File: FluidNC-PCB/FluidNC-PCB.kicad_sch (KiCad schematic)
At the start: 0 parts

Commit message: First steps!
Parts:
- added A1: Pololu_Breakout_A4988, Module:Pololu_Breakout-16_15.2x20.3mm, symbol Driver_Motor:Pololu_Breakout_A4988
- added J1: Conn_01x04_Pin, symbol Connector:Conn_01x04_Pin
- added R2, R3, R4: R, symbol Device:R
- added SW1: SW_DIP_x04, Button_Switch_THT:SW_DIP_SPSTx04_Slide_9.78x12.34mm_W7.62mm_P2.54mm, symbol Switch:SW_DIP_x04
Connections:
- new net: A1.10 (MS1), R2.1, SW1.6
- new net: A1.11 (MS2), R3.1, SW1.7
- new net: A1.12 (MS3), R4.1, SW1.8
- new net: A1.3 (1B), J1.4 (Pin_4)
- new net: A1.4 (1A), J1.3 (Pin_3)
- new net: A1.5 (2A), J1.2 (Pin_2)
- new net: A1.6 (2B), J1.1 (Pin_1)
- new net +12V: A1.8 (VMOT)
- new net +3.3V: A1.13 (~{RESET}), A1.14 (~{SLEEP}), A1.2 (VDD)
- new net ENABLE_N: A1.9 (~{ENABLE})
- new net GND: A1.1 (GND), A1.7 (GND), R2.2, R3.2, R4.2
- no-connect marks 0 -> 2

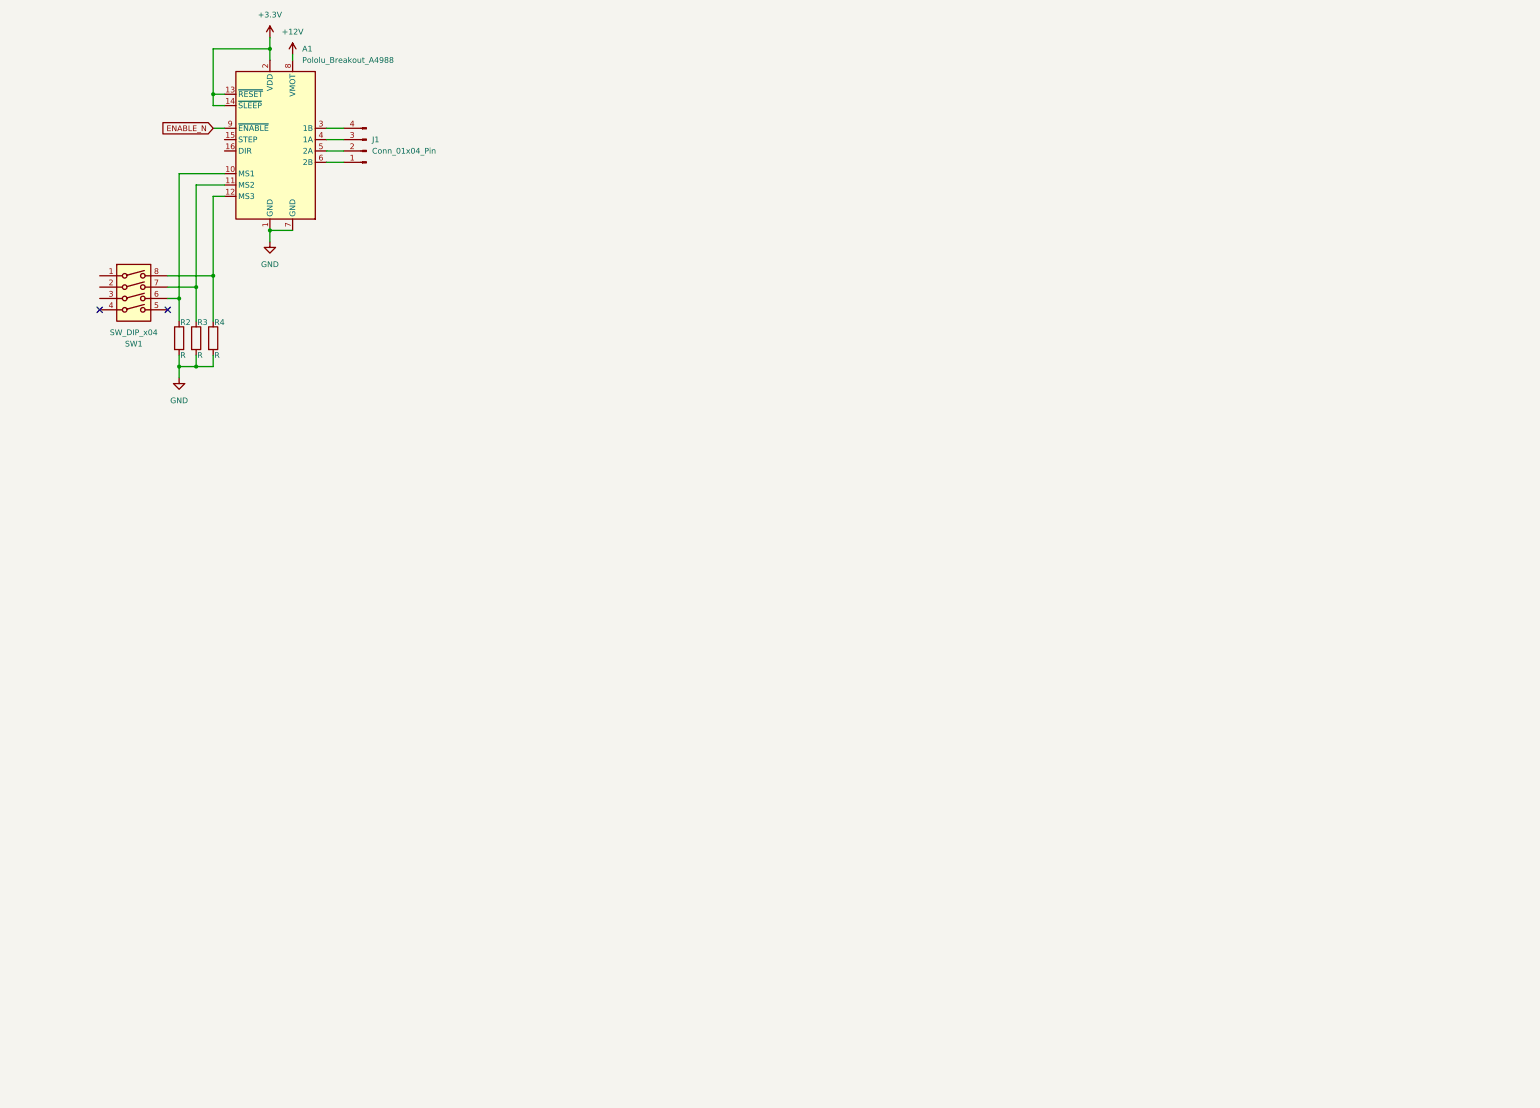
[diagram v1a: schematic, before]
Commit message: Added ESP32 plotter symbol to schematic and repo (moved from template). Started uC wiring.
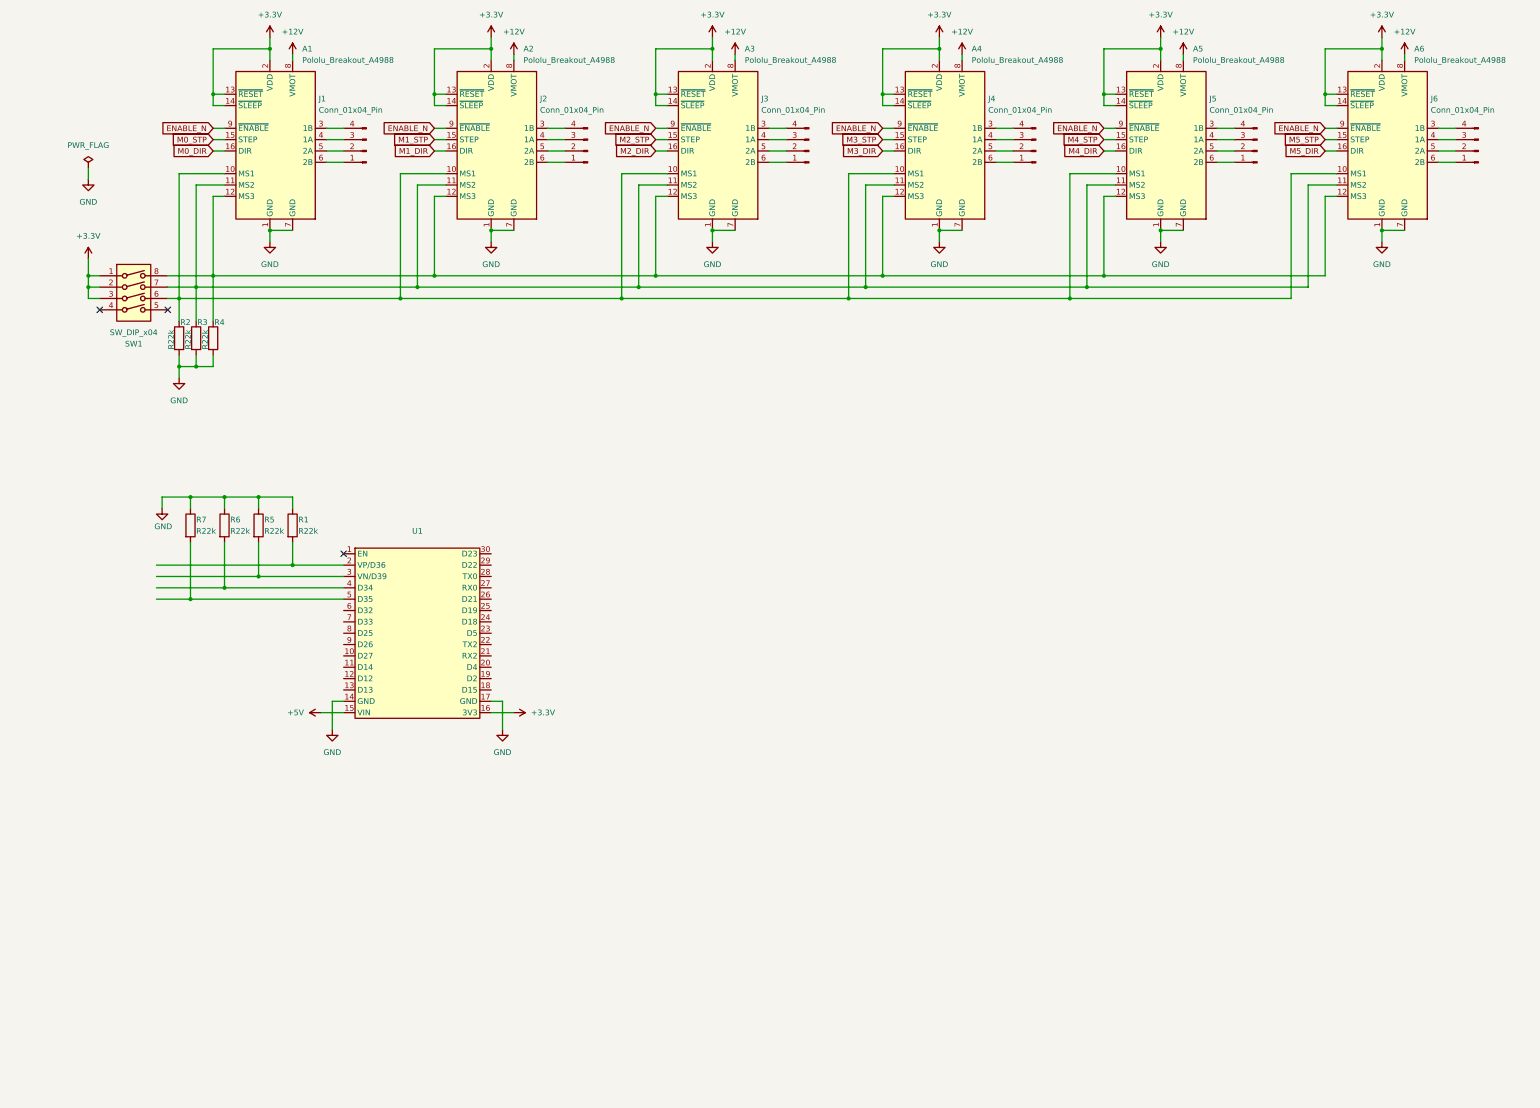
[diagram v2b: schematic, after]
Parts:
- added A2, A3, A4, A5, A6: Pololu_Breakout_A4988, Module:Pololu_Breakout-16_15.2x20.3mm, symbol Driver_Motor:Pololu_Breakout_A4988
- added J2, J3, J4, J5, J6: Conn_01x04_Pin, symbol Connector:Conn_01x04_Pin
- added R1, R5, R6, R7: R22k, symbol Device:R
- added U1: ~, plotter:esp32-mystery-footprint, symbol plotter:esp32_wroom_doit_devB
- R2, R3, R4: value R -> R22k
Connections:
- net +12V: now also A2.8 (VMOT), A3.8 (VMOT), A4.8 (VMOT), A5.8 (VMOT), A6.8 (VMOT)
- net +3.3V: now also SW1.1, SW1.2, SW1.3, A2.13 (~{RESET}), A2.14 (~{SLEEP}), A2.2 (VDD), A3.13 (~{RESET}), A3.14 (~{SLEEP}), A3.2 (VDD), A4.13 (~{RESET}), A4.14 (~{SLEEP}), A4.2 (VDD), A5.13 (~{RESET}), A5.14 (~{SLEEP}), A5.2 (VDD), A6.13 (~{RESET}), A6.14 (~{SLEEP}), A6.2 (VDD), U1.16 (3V3)
- net ENABLE_N: now also A2.9 (~{ENABLE}), A3.9 (~{ENABLE}), A4.9 (~{ENABLE}), A5.9 (~{ENABLE}), A6.9 (~{ENABLE})
- net GND: now also A2.1 (GND), A2.7 (GND), A3.1 (GND), A3.7 (GND), A4.1 (GND), A4.7 (GND), A5.1 (GND), A5.7 (GND), A6.1 (GND), A6.7 (GND), R1.1, R5.1, R6.1, R7.1, U1.14 (GND), U1.17 (GND)
- net at A1.10 (MS1), R2.1, SW1.6: now also A2.10 (MS1), A3.10 (MS1), A4.10 (MS1), A5.10 (MS1), A6.10 (MS1)
- net at A1.11 (MS2), R3.1, SW1.7: now also A2.11 (MS2), A3.11 (MS2), A4.11 (MS2), A5.11 (MS2), A6.11 (MS2)
- net at A1.12 (MS3), R4.1, SW1.8: now also A2.12 (MS3), A3.12 (MS3), A4.12 (MS3), A5.12 (MS3), A6.12 (MS3)
- net M0_STP: now reaches A1.15 (STEP)
- net M0_DIR: now reaches A1.16 (DIR)
- new net: R7.2, U1.5 (D35)
- new net: A2.3 (1B), J2.4 (Pin_4)
- new net: A2.4 (1A), J2.3 (Pin_3)
- new net: A2.5 (2A), J2.2 (Pin_2)
- new net: A2.6 (2B), J2.1 (Pin_1)
- new net: R1.2, U1.2 (VP/D36)
- new net: A4.6 (2B), J4.1 (Pin_1)
- new net: A4.5 (2A), J4.2 (Pin_2)
- new net: A4.4 (1A), J4.3 (Pin_3)
- new net: A4.3 (1B), J4.4 (Pin_4)
- new net: A6.3 (1B), J6.4 (Pin_4)
- new net: A6.4 (1A), J6.3 (Pin_3)
- new net: A6.5 (2A), J6.2 (Pin_2)
- new net: A6.6 (2B), J6.1 (Pin_1)
- new net: R5.2, U1.3 (VN/D39)
- new net: R6.2, U1.4 (D34)
- new net: A5.6 (2B), J5.1 (Pin_1)
- new net: A5.5 (2A), J5.2 (Pin_2)
- new net: A5.4 (1A), J5.3 (Pin_3)
- new net: A5.3 (1B), J5.4 (Pin_4)
- new net: A3.6 (2B), J3.1 (Pin_1)
- new net: A3.5 (2A), J3.2 (Pin_2)
- new net: A3.4 (1A), J3.3 (Pin_3)
- new net: A3.3 (1B), J3.4 (Pin_4)
- new net +5V: U1.15 (VIN)
- new net M1_DIR: A2.16 (DIR)
- new net M1_STP: A2.15 (STEP)
- new net M2_DIR: A3.16 (DIR)
- new net M2_STP: A3.15 (STEP)
- new net M3_DIR: A4.16 (DIR)
- new net M3_STP: A4.15 (STEP)
- new net M4_DIR: A5.16 (DIR)
- new net M4_STP: A5.15 (STEP)
- new net M5_DIR: A6.16 (DIR)
- new net M5_STP: A6.15 (STEP)
- no-connect marks 2 -> 3

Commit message: Mostly done PCB :)
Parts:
- removed U1: ~, plotter:esp32-mystery-footprint, symbol plotter:esp32_wroom_doit_devB
- added C1, C14, C2, C3, C4, C5, C6: 33uF, Capacitor_THT:C_Radial_D8.0mm_H11.5mm_P3.50mm, symbol Device:C
- added C10, C11, C12, C13, C7, C8, C9: 100nF, Capacitor_THT:C_Disc_D4.3mm_W1.9mm_P5.00mm, symbol Device:C
- added H1, H2, H3, H4, H5, H6: MountingHole, MountingHole:MountingHole_3.2mm_M3, symbol Mechanical:MountingHole
- added J11, J12, J13, J14, J15, J16, J17, J18, J19: Molex_01x02_Socket, Connector_Molex:Molex_KK-254_AE-6410-02A_1x02_P2.54mm_Vertical, symbol Connector:Conn_01x02_Socket
- added J7: 12V Power Input, TerminalBlock_Phoenix:TerminalBlock_Phoenix_MKDS-1,5-2_1x02_P5.00mm_Horizontal, symbol Connector:Screw_Terminal_01x02
- added J8: Fan Screw Terminal, TerminalBlock_Phoenix:TerminalBlock_Phoenix_MKDS-1,5-2_1x02_P5.00mm_Horizontal, symbol Connector:Screw_Terminal_01x02
- added R8, R9: R22k, Resistor_THT:R_Axial_DIN0207_L6.3mm_D2.5mm_P5.08mm_Vertical, symbol Device:R
- added U2: ~, plotter:esp32-mystery-footprint, symbol plotter:esp32_wroom_doit_devB
- J1, J2, J3, J4, J5, J6: footprint (none) -> Connector_Molex:Molex_KK-254_AE-6410-04A_1x04_P2.54mm_Vertical
- R1, R2, R3, R4, R5, R6, R7: footprint (none) -> Resistor_THT:R_Axial_DIN0207_L6.3mm_D2.5mm_P5.08mm_Vertical
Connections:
- net +12V: now also C1.1, C14.1, C2.1, C3.1, C4.1, C5.1, C6.1, J17.1 (Pin_1), J7.1 (Pin_1), J8.1 (Pin_1)
- net +3.3V: now also C10.1, C11.1, C12.1, C7.1, C8.1, C9.1, J11.1 (Pin_1), J12.1 (Pin_1), J13.1 (Pin_1), J14.1 (Pin_1), J15.1 (Pin_1), J16.1 (Pin_1), U2.16 (3V3)
- net +5V: now also C13.1, J18.1 (Pin_1), U2.15 (VIN)
- net ENABLE_N: now also U2.20 (D4)
- net GND: now also C1.2, C10.2, C11.2, C12.2, C13.2, C14.2, C2.2, C3.2, C4.2, C5.2, C6.2, C7.2, C8.2, C9.2, J17.2 (Pin_2), J18.2 (Pin_2), J7.2 (Pin_2), J8.2 (Pin_2), R8.2, R9.2, U2.14 (GND), U2.17 (GND)
- net M0_DIR: now also U2.6 (D32)
- net M0_STP: now also U2.7 (D33)
- net M1_DIR: now also U2.8 (D25)
- net M1_STP: now also U2.9 (D26)
- net M2_DIR: now also U2.10 (D27)
- net M2_STP: now also U2.11 (D14)
- net M3_DIR: now also U2.12 (D12)
- net M3_STP: now also U2.13 (D13)
- net M4_DIR: now also U2.30 (D23)
- net M4_STP: now also U2.29 (D22)
- net M5_DIR: now also U2.26 (D21)
- net M5_STP: now also U2.25 (D19)
- net at R7.2: now also J14.2 (Pin_2), U2.5 (D35)
- net at R1.2: now also J11.2 (Pin_2), U2.2 (VP/D36)
- net at R5.2: now also J12.2 (Pin_2), U2.3 (VN/D39)
- net at R6.2: now also J13.2 (Pin_2), U2.4 (D34)
- new net: J16.2 (Pin_2), R9.1, U2.19 (D2)
- new net: J15.2 (Pin_2), R8.1, U2.18 (D15)
- new net: J19.2 (Pin_2), U2.23 (D5)
- new net: J19.1 (Pin_1), U2.24 (D18)
- no-connect marks 3 -> 7
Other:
- note added: "Caps on drivers, uC, big caps on 12V!"
- moved on the sheet: R1, R5, R6, R7

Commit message: Finished (version 1) of PCB
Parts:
- removed H5, H6: MountingHole, MountingHole:MountingHole_3.2mm_M3, symbol Mechanical:MountingHole
- removed J19: Molex_01x02_Socket, Connector_Molex:Molex_KK-254_AE-6410-02A_1x02_P2.54mm_Vertical, symbol Connector:Conn_01x02_Socket
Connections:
- net M0_DIR: now also U2.8 (D25); no longer U2.6 (D32)
- net M0_STP: now also U2.9 (D26); no longer U2.7 (D33)
- net M1_DIR: now also U2.10 (D27); no longer U2.8 (D25)
- net M1_STP: now also U2.11 (D14); no longer U2.9 (D26)
- net M2_DIR: now also U2.12 (D12); no longer U2.10 (D27)
- net M2_STP: now also U2.13 (D13); no longer U2.11 (D14)
- net M3_DIR: now also U2.6 (D32); no longer U2.12 (D12)
- net M3_STP: now also U2.7 (D33); no longer U2.13 (D13)
- net M4_DIR: now also U2.29 (D22); no longer U2.30 (D23)
- net M4_STP: now also U2.30 (D23); no longer U2.29 (D22)
- net M5_DIR: now also U2.25 (D19); no longer U2.26 (D21)
- net M5_STP: now also U2.26 (D21); no longer U2.25 (D19)
- no-connect marks 7 -> 9

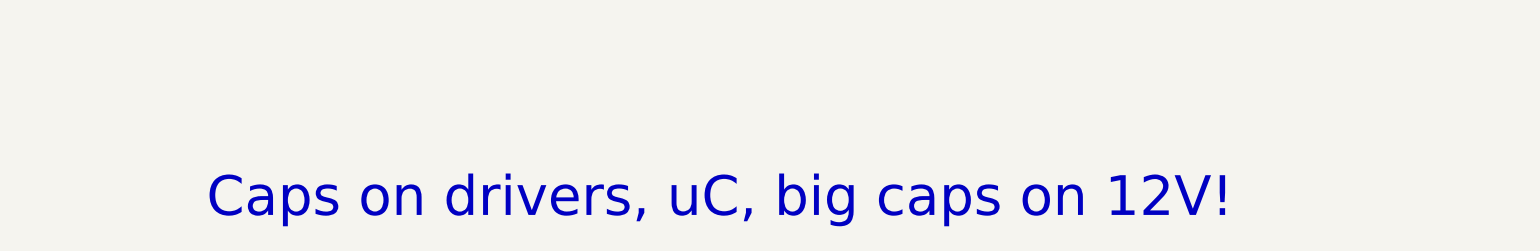
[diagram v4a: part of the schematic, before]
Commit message: Added schematic PDF and PNG of PCB layout
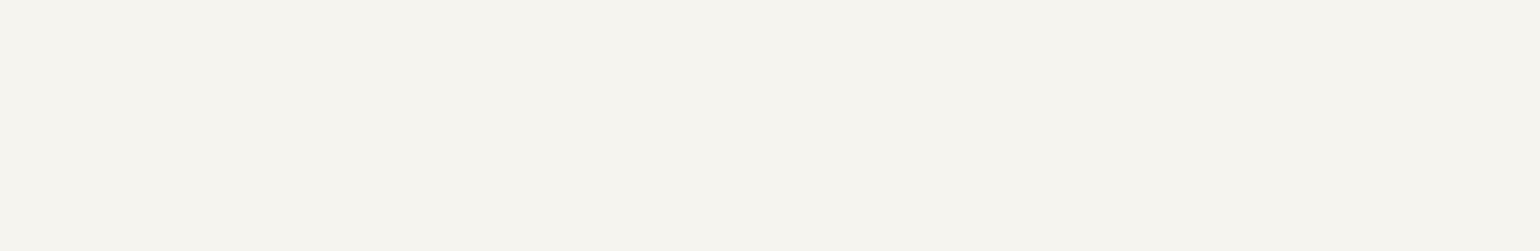
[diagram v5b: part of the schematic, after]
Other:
- note removed: "Caps on drivers, uC, big caps on 12V!"
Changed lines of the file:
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@@
 	(generator_version "9.0")
 	(paper "A3")
-	(text "Caps on drivers, uC, big caps on 12V!"
-		(exclude_from_sim no)
-		(at 120.65 254 0)
-		(effects
-			(font
-				(size 6.35 6.35)
-			)
-		)
-	)
 	(junction
 		(at 212.09 184.15)
